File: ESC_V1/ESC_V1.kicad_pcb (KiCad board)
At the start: 2 copper layers, 58 x 20 mm, 27 parts, among them J1 Conn_01x06_Female, J2 Conn_01x03_Female, J3 Conn_01x02_Female, Q1 NPN Transistor 40V, Q10 NPN Transistor 40V, Q11 P Channel 40V 30A, Q12 N Channel 40V 30A, Q2 NPN Transistor 40V, Q3 P Channel 40V 30A, Q4 N Channel 40V 30A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

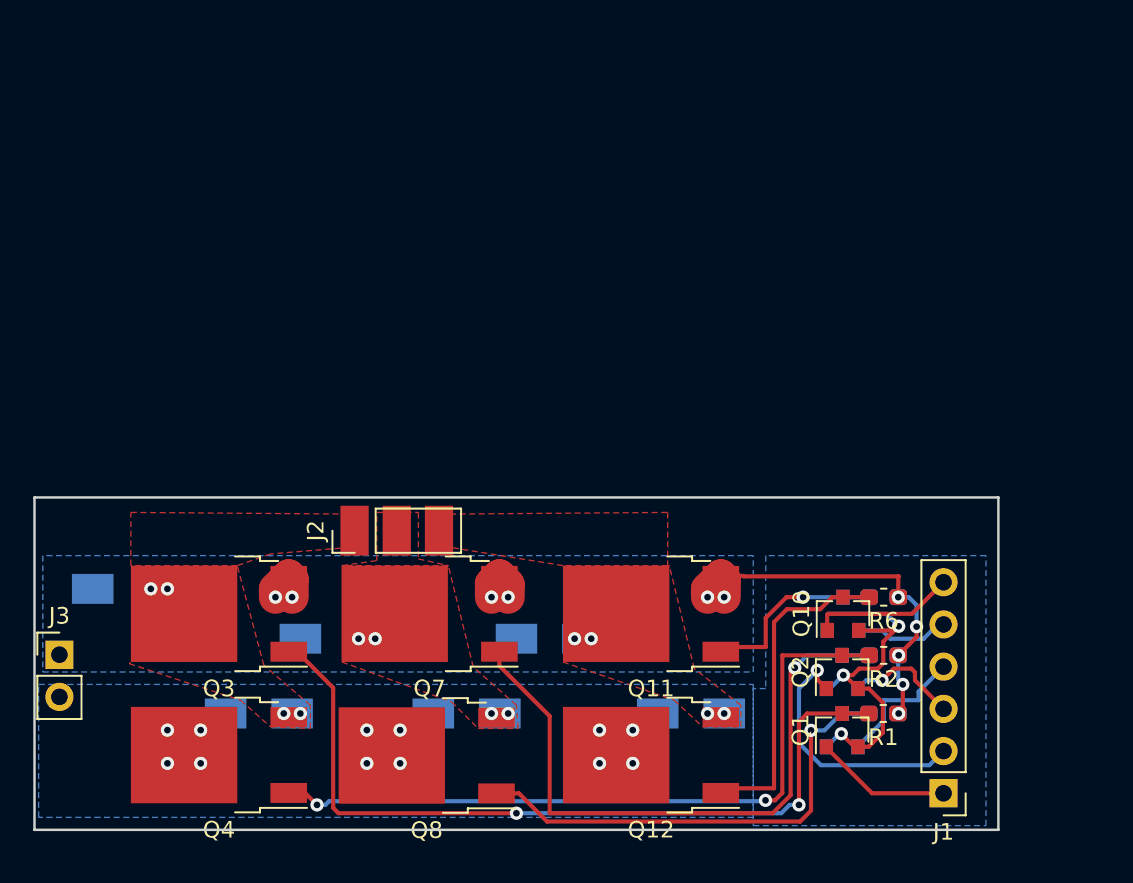
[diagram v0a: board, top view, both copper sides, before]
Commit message: Board v2 with darlington array and higher current capacity
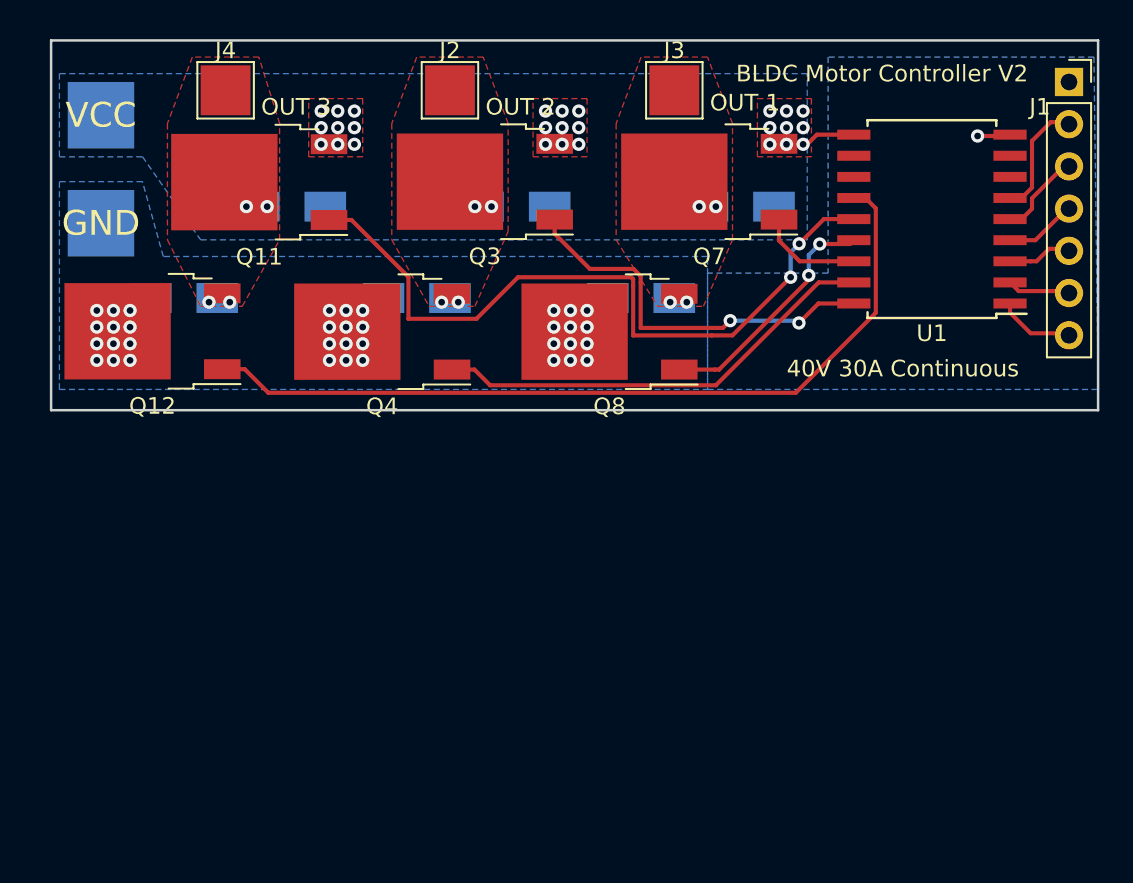
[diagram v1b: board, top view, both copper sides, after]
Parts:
- removed Q1, Q10, Q2, Q5, Q6, Q9: NPN Transistor 40V, Package_TO_SOT_SMD:SOT-23
- removed R1, R2, R3, R4, R5, R6: 10k, Resistor_SMD:R_0603_1608Metric_Pad1.05x0.95mm_HandSolder
- added J4: Conn_01x01_Female, TestPoint:TestPoint_Pad_3.0x3.0mm, F.Cu at (132.5, 51.5)
- added J5: Conn_01x01_Female, TestPoint:TestPoint_Pad_4.0x4.0mm, B.Cu at (125.0, 53.0)
- added J6: Conn_01x01_Female, TestPoint:TestPoint_Pad_4.0x4.0mm, B.Cu at (125.0, 59.5)
- added U1: ULN2803A, Package_SO:SOIC-18W_7.5x11.6mm_P1.27mm, F.Cu at (175.0, 59.2)
- J1: value Conn_01x06_Female -> Conn_01x07_Female; footprint Connector_PinHeader_2.54mm:PinHeader_1x06_P2.54mm_Vertical -> Connector_PinSocket_2.54mm:PinSocket_1x07_P2.54mm_Vertical
- J2: value Conn_01x03_Female -> Conn_01x01_Female; footprint Connector_PinHeader_2.54mm:PinHeader_1x03_P2.54mm_Vertical -> TestPoint:TestPoint_Pad_3.0x3.0mm
- J3: value Conn_01x02_Female -> Conn_01x01_Female; footprint Connector_PinHeader_2.54mm:PinHeader_1x02_P2.54mm_Vertical -> TestPoint:TestPoint_Pad_3.0x3.0mm
- moved J3 50.2 mm to (159.5, 51.5)
- moved J1 43.5 mm to (183.2, 51.0), turned to 0 degrees
- moved D6 39.4 mm to (130.0, 64.0)
- moved Q12 39.4 mm to (128.1, 66.0)
- moved D3 35.7 mm to (163.5, 58.5), turned to 180 degrees
- moved Q11 35.1 mm to (134.5, 57.0)
- moved D1 32.9 mm to (150.0, 58.5), turned to 180 degrees
- moved Q7 31.0 mm to (161.6, 57.0)
- moved Q3 30.5 mm to (148.1, 57.0)
- moved D5 30.3 mm to (136.5, 58.5), turned to 180 degrees
- moved Q8 27.8 mm to (155.6, 66.0)
- moved Q4 27.3 mm to (141.9, 66.0)
- moved D4 27.1 mm to (157.5, 64.0)
- moved J2 27.1 mm to (146.0, 51.5), turned to 0 degrees
- moved D2 26.7 mm to (144.0, 64.0)
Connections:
- D1 pad 2: OUT1 -> MOTOR1
- D2 pad 1: OUT1 -> MOTOR1
- D3 pad 2: OUT2 -> MOTOR2
- D4 pad 1: OUT2 -> MOTOR2
- D5 pad 2: OUT3 -> MOTOR3
- D6 pad 1: OUT3 -> MOTOR3
- J1 pad 1: IN1 -> GND
- J1 pad 2: IN2 -> Net-(J1-Pad2)
- J1 pad 3: IN3 -> Net-(J1-Pad3)
- J1 pad 4: IN4 -> Net-(J1-Pad4)
- J1 pad 5: IN5 -> Net-(J1-Pad5)
- J1 pad 6: IN6 -> Net-(J1-Pad6)
- J2 pad 1: OUT1 -> MOTOR1
- J3 pad 1: VCC -> MOTOR2
- Q11 pad 1: Net-(Q11-Pad1) -> OUT5
- Q11 pad 2: OUT3 -> MOTOR3
- Q12 pad 1: Net-(Q10-Pad3) -> OUT6
- Q12 pad 3: OUT3 -> MOTOR3
- Q3 pad 1: Net-(Q1-Pad3) -> OUT1
- Q3 pad 2: OUT1 -> MOTOR1
- Q4 pad 1: Net-(Q2-Pad3) -> OUT2
- Q4 pad 3: OUT1 -> MOTOR1
- Q7 pad 1: Net-(Q5-Pad3) -> OUT3
- Q7 pad 2: OUT2 -> MOTOR2
- Q8 pad 1: Net-(Q6-Pad3) -> OUT4
- Q8 pad 3: OUT2 -> MOTOR2
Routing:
- net OUT6: track 0.00 -> 49.8 mm
- net Net-(Q1-Pad3): track 48.6 -> 0.00 mm, vias 2 -> 0
- net Net-(Q2-Pad3): track 44.3 -> 0.00 mm, vias 2 -> 0
- net OUT5: track 0.00 -> 43.8 mm, vias 0 -> 2
- net Net-(Q5-Pad3): track 38.5 -> 0.00 mm, vias 1 -> 0
- net Net-(Q6-Pad3): track 28.9 -> 0.00 mm, vias 1 -> 0
- net OUT2: track 0.00 -> 27.1 mm, vias 4 -> 0
- net VCC: track 29.4 -> 4.29 mm, vias 11 -> 27
- net OUT1: track 0.20 -> 23.7 mm, vias 4 -> 2
- net GND: track 23.0 -> 1.98 mm, vias 15 -> 37
- net Net-(Q10-Pad3): track 19.7 -> 0.00 mm
- net IN2: track 15.8 -> 0.00 mm, vias 1 -> 0
- net OUT4: track 0.00 -> 14.6 mm, vias 0 -> 2
- net Net-(Q11-Pad1): track 11.3 -> 0.00 mm, vias 1 -> 0
- net IN6: track 8.81 -> 0.00 mm
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- added copper zone on F.Cu, net MOTOR1
- added copper zone on F.Cu, net MOTOR2
- added copper zone on F.Cu, net MOTOR3
- added copper zone on F.Cu, net VCC
- removed copper zone on F.Cu, net OUT1
- removed copper zone on F.Cu, net OUT2
- removed copper zone on F.Cu, net OUT3
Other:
- board size 58 x 20 mm -> 63 x 22.2 mm
- board text added: "40V 30A Continuous"
- board text added: "BLDC Motor Controller V2"
- board text added: "G"
- board text added: "GND"
- board text added: "OUT 1"
- board text added: "OUT 2"
- board text added: "OUT 3"
- board text added: "VCC"
